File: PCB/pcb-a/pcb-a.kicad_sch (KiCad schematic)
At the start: 14 parts, among them Q1 BC807, Q3 BC817, SW1 config, U1 ESP32-S2-DevKitM

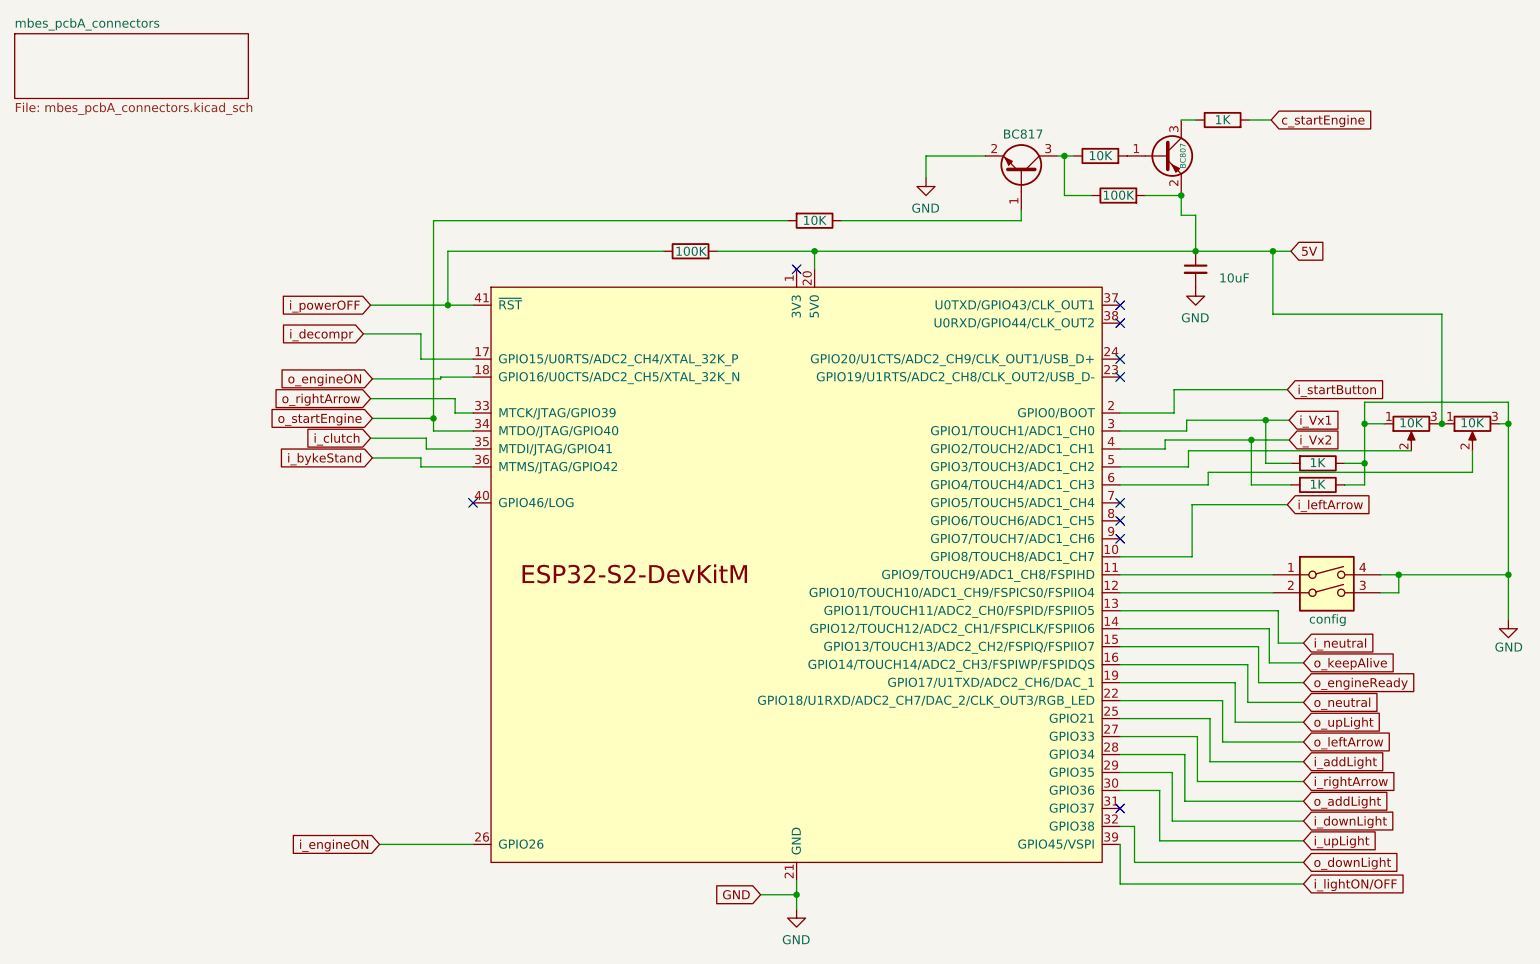
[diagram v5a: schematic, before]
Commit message: Many changes and fixes
Electric schema A & B
	- Wrong (undefined) signals direction fixed
	- More readable schema getting: c_<signal> color has changed
	- Some pull-up resistors has been added for safing purpose
	- Wire connectors holes size reducing
	- Because Led indicatord uses less then 500mA, their wire connectors have been substituted by pin-header ones

PCB
	- Updates for schema changes
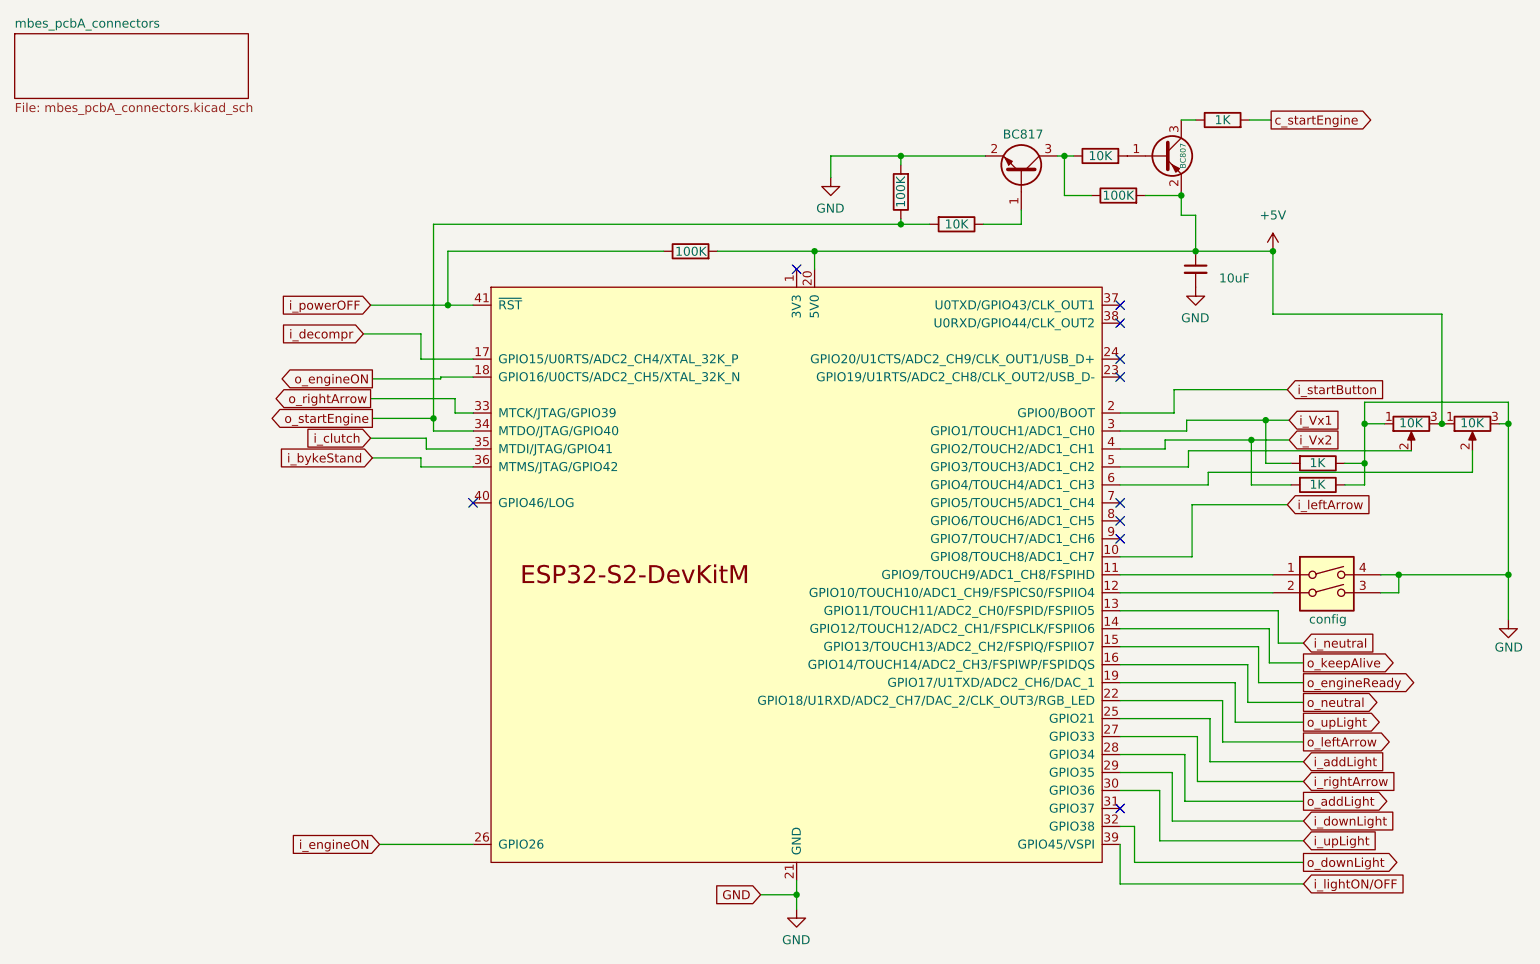
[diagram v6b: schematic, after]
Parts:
- added R21: 100K, Resistor_SMD:R_1206_3216Metric, symbol Device:R
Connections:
- net GND: now also R21.2
- net o_startEngine: now also R21.1
- net 5V renamed +5V

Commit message: Small changes for the Title block
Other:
- company: Panicosoft -> https://github.com/catinella/mbElectricalSystem
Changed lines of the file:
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@@
 	(title_block
 		(title "Motorbike lights and services controller")
-		(date "2022-08-24")
-		(rev "4.0")
-		(company "Panicosoft")
-		(comment 1 "Logic controller unit")
-		(comment 2 "MCU connections")
+		(company "https://github.com/catinella/mbElectricalSystem")
 	)
 	(bus_alias "port-b"

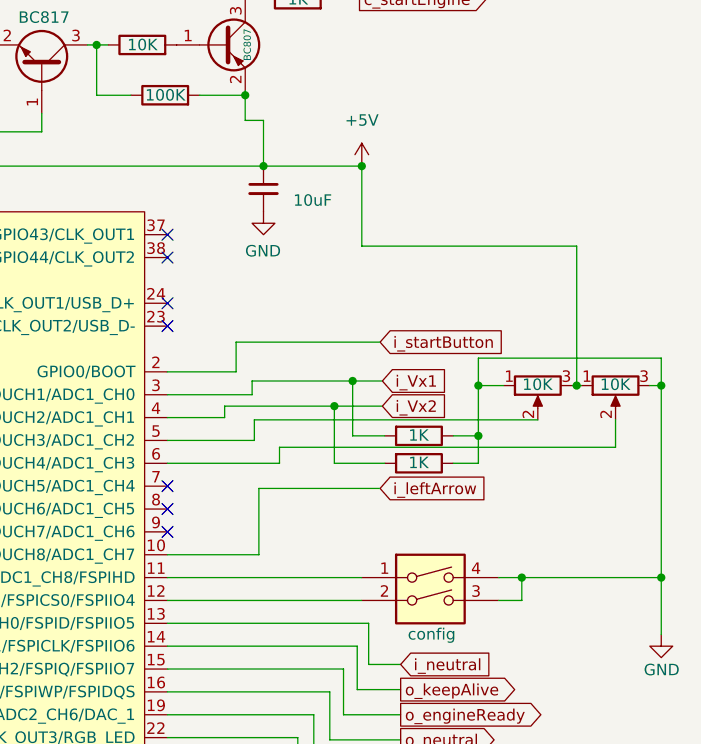
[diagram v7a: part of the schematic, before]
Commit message: Merging from main
Key authentication physical references removed
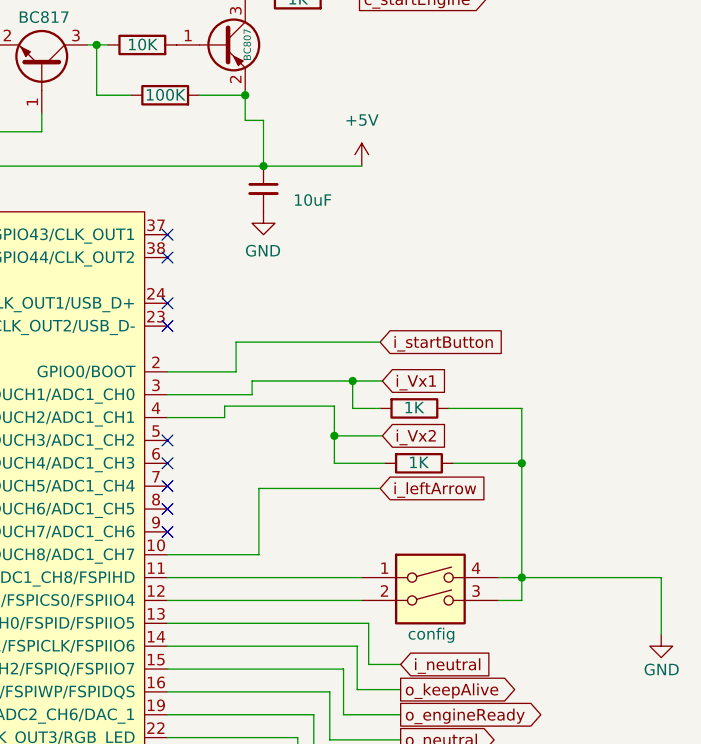
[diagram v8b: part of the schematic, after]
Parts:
- removed RV1, RV2: 10K, Potentiometer_THT:Potentiometer_Bourns_3296W_Vertical, symbol Device:R_Potentiometer
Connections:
- no-connect marks 10 -> 12
